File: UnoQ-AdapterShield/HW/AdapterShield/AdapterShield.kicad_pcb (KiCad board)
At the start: 2 copper layers, 89 x 53.3 mm, 12 parts, among them J3 Conn_02x10_Odd_Even, J4 Conn_02x12_Odd_Even

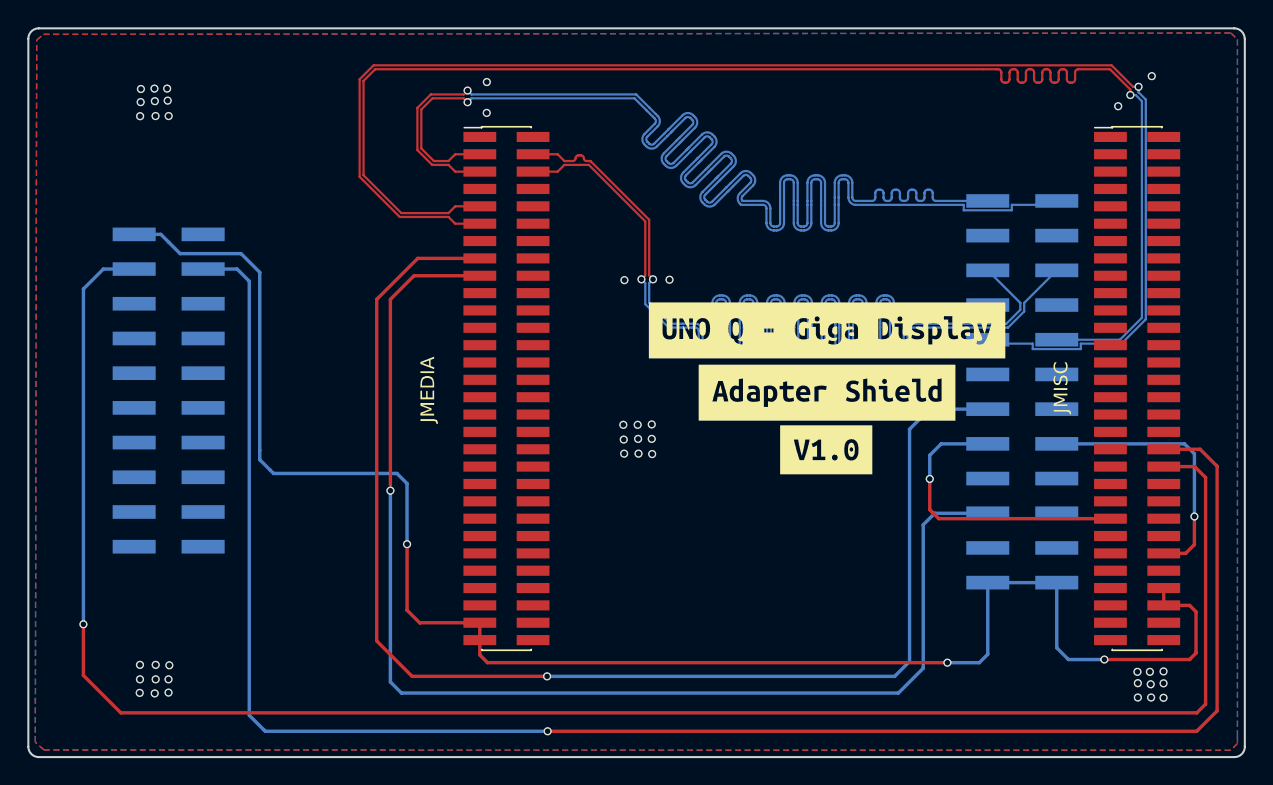
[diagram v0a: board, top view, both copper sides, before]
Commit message: fix(Hw):Improved_MIPI_routing
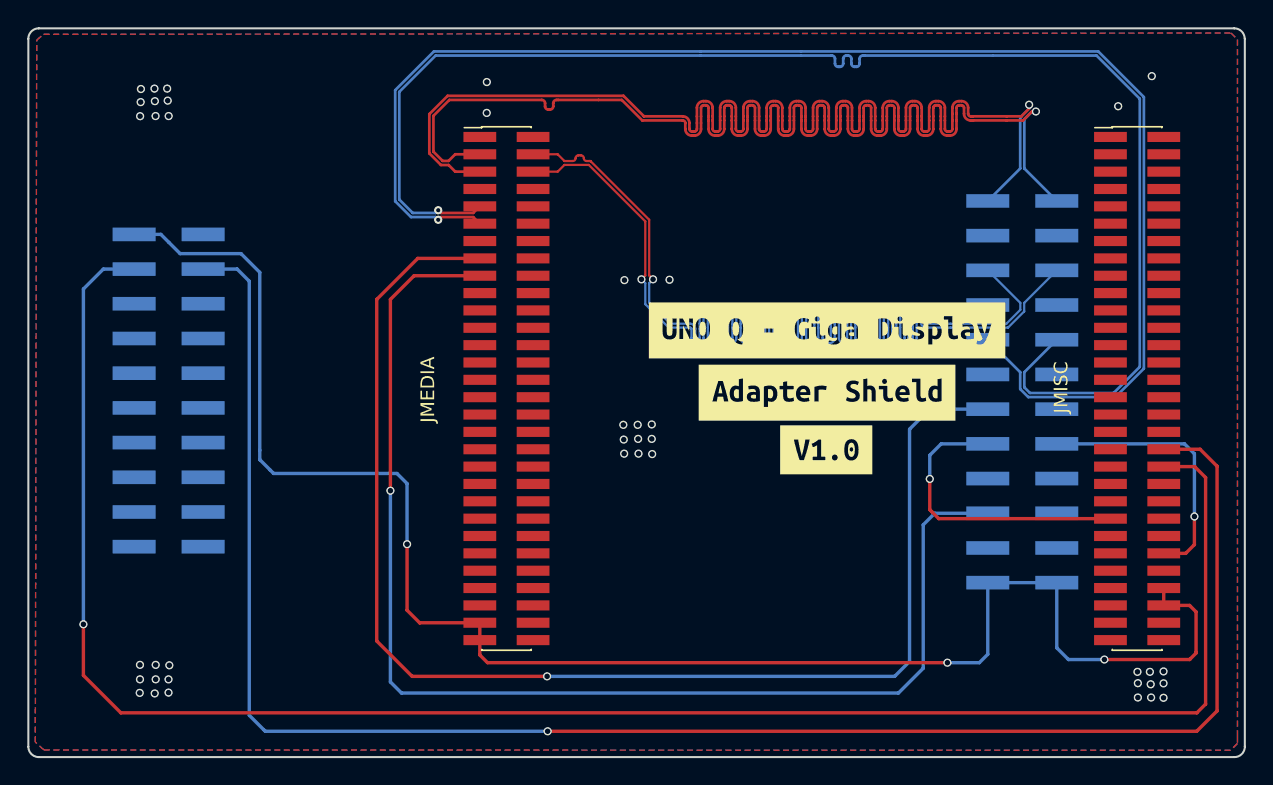
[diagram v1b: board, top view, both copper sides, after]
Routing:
- net /MIPI_D0P: track 105.6 -> 107.1 mm
- net /MIPI_D1N: track 105.1 -> 106.5 mm
- net /MIPI_CLKN: track 105.3 -> 106.6 mm
- net /MIPI_CLKP: track 105.3 -> 106.6 mm
- net /MIPI_D0N: track 105.9 -> 107.2 mm
- net /MIPI_D1P: track 105.4 -> 106.4 mm
